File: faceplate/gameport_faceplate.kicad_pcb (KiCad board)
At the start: 2 copper layers, 25 x 200 mm, 5 parts

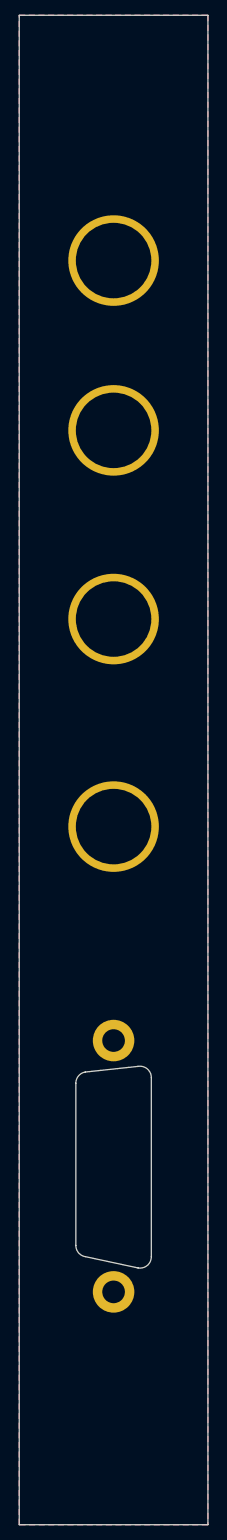
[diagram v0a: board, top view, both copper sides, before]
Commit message: Complete faceplate
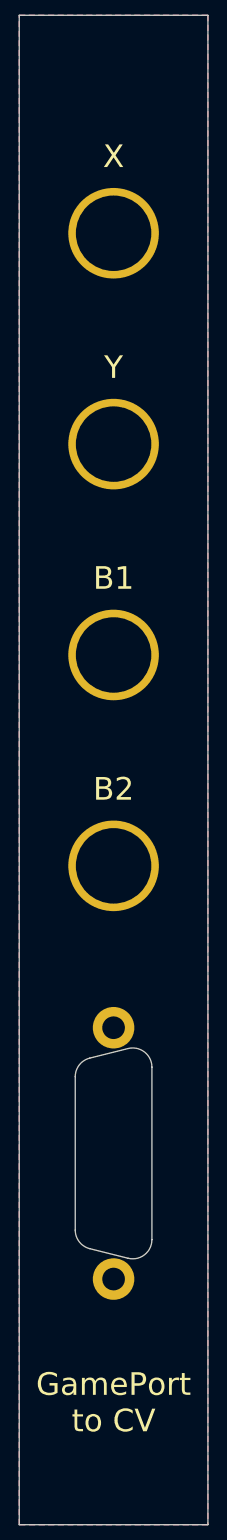
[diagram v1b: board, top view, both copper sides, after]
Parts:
- moved H4 5.20 mm to (112.5, 137.7)
- moved H3 4.76 mm to (112.5, 109.8)
- moved H1 3.62 mm to (112.5, 53.9)
- moved H2 1.82 mm to (112.5, 81.8)
- moved H5 1.70 mm to (112.5, 175.8)
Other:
- outline, holes or cut-outs redrawn
- board text added: "B1"
- board text added: "B2"
- board text added: "GamePort to CV"
- board text added: "JLCJLCJLCJLC"
- board text added: "X"
- board text added: "Y"
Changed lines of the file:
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@@
   (general
     (thickness 1.6)
-    (drawings 18)
+    (drawings 26)
     (tracks 0)
     (zones 0)
@@
   )
   (module modular:DSub_15_Cutout (layer F.Cu)
-    (at 112.5 177.5)
+    (at 112.5 175.8)
     (fp_text reference H5 (at 0 20) (layer F.SilkS) hide
       (effects (font (size 1 1) (thickness 0.15)))
@@
   )
   (module modular:Jack (layer F.Cu)
-    (at 112.5 132.5)
+    (at 112.5 137.7)
     (fp_text reference H4 (at 0 7.5) (layer F.SilkS) hide
       (effects (font (size 1 1) (thickness 0.15)))
@@
   )
   (module modular:Jack (layer F.Cu)
-    (at 112.5 105)
+    (at 112.5 109.76)
     (fp_text reference H3 (at 0 7.5) (layer F.SilkS) hide
       (effects (font (size 1 1) (thickness 0.15)))
@@
   )
   (module modular:Jack (layer F.Cu)
-    (at 112.5 80)
+    (at 112.5 81.82)
     (fp_text reference H2 (at 0 7.5) (layer F.SilkS) hide
       (effects (font (size 1 1) (thickness 0.15)))
@@
   )
   (module modular:Jack (layer F.Cu)
-    (at 112.5 57.5)
+    (at 112.5 53.88)
     (fp_text reference H1 (at 0 7.5) (layer F.SilkS) hide
       (effects (font (size 1 1) (thickness 0.15)))
@@
       (net 1 GND))
   )
-  (gr_line (start 100 177.5) (end 125 177.5) (layer Dwgs.User) (width 0.15))
-  (gr_arc (start 120.25 188.5) (end 122.25 188.5) (angle 100) (layer Dwgs.User) (width 0.05))
-  (gr_arc (start 116 165.75) (end 117.5 165.75) (angle -100) (layer Edge.Cuts) (width 0.05))
-  (gr_arc (start 109 166.5) (end 107.5 166.5) (angle 80) (layer Edge.Cuts) (width 0.05))
-  (gr_arc (start 109 188) (end 107.5 188) (angle -80) (layer Edge.Cuts) (width 0.05))
-  (gr_arc (start 116 189.5) (end 117.5 189.5) (angle 100) (layer Edge.Cuts) (width 0.05))
-  (gr_line (start 100 125) (end 125 125) (layer Dwgs.User) (width 0.15))
-  (gr_line (start 108.739528 165.022788) (end 115.739528 164.272788) (layer Edge.Cuts) (width 0.05))
-  (gr_line (start 107.5 188) (end 107.5 166.5) (layer Edge.Cuts) (width 0.05))
-  (gr_line (start 115.739528 190.977212) (end 108.739528 189.477212) (layer Edge.Cuts) (width 0.05))
-  (gr_line (start 117.5 165.75) (end 117.5 189.5) (layer Edge.Cuts) (width 0.05))
+  (gr_text JLCJLCJLCJLC (at 122.66 125 270) (layer B.SilkS)
+    (effects (font (size 1 1) (thickness 0.15)) (justify mirror))
+  )
+  (gr_text "GamePort\nto CV" (at 112.5 208.82) (layer F.SilkS)
+    (effects (font (size 3 3) (thickness 0.5)))
+  )
+  (gr_text B2 (at 112.5 127.54) (layer F.SilkS)
+    (effects (font (size 3 3) (thickness 0.45)))
+  )
+  (gr_text B1 (at 112.5 99.6) (layer F.SilkS)
+    (effects (font (size 3 3) (thickness 0.45)))
+  )
+  (gr_text Y (at 112.5 71.66) (layer F.SilkS)
+    (effects (font (size 3 3) (thickness 0.45)))
+  )
+  (gr_text X (at 112.5 43.72) (layer F.SilkS)
+    (effects (font (size 3 3) (thickness 0.45)))
+  )
+  (dimension 27.94 (width 0.15) (layer Dwgs.User)
+    (gr_text "1.1000 in" (at 121.42 175.8 90) (layer Dwgs.User)
+      (effects (font (size 1 1) (thickness 0.15)))
+    )
+    (feature1 (pts (xy 115.04 161.83) (xy 120.706421 161.83)))
+    (feature2 (pts (xy 115.04 189.77) (xy 120.706421 189.77)))
+    (crossbar (pts (xy 120.12 189.77) (xy 120.12 161.83)))
+    (arrow1a (pts (xy 120.12 161.83) (xy 120.706421 162.956504)))
+    (arrow1b (pts (xy 120.12 161.83) (xy 119.533579 162.956504)))
+    (arrow2a (pts (xy 120.12 189.77) (xy 120.706421 188.643496)))
+    (arrow2b (pts (xy 120.12 189.77) (xy 119.533579 188.643496)))
+  )
+  (dimension 33.02 (width 0.15) (layer Dwgs.User)
+    (gr_text "1.3000 in" (at 103.58 175.8 90) (layer Dwgs.User)
+      (effects (font (size 1 1) (thickness 0.15)))
+    )
+    (feature1 (pts (xy 112.5 159.29) (xy 104.293579 159.29)))
+    (feature2 (pts (xy 112.5 192.31) (xy 104.293579 192.31)))
+    (crossbar (pts (xy 104.88 192.31) (xy 104.88 159.29)))
+    (arrow1a (pts (xy 104.88 159.29) (xy 105.466421 160.416504)))
+    (arrow1b (pts (xy 104.88 159.29) (xy 104.293579 160.416504)))
+    (arrow2a (pts (xy 104.88 192.31) (xy 105.466421 191.183496)))
+    (arrow2b (pts (xy 104.88 192.31) (xy 104.293579 191.183496)))
+  )
+  (gr_line (start 109.343961 163.175839) (end 114.42396 161.905838) (layer Edge.Cuts) (width 0.05))
+  (gr_arc (start 109.96 165.64) (end 109.343961 163.175839) (angle -75.96376747) (layer Edge.Cuts) (width 0.05))
+  (gr_arc (start 115.04 164.37) (end 117.58 164.37) (angle -104.0362435) (layer Edge.Cuts) (width 0.05))
+  (gr_line (start 109.345518 188.424551) (end 114.423961 189.694161) (layer Edge.Cuts) (width 0.05))
+  (gr_arc (start 115.04 187.23) (end 114.423961 189.694161) (angle -104.0362325) (layer Edge.Cuts) (width 0.05))
+  (gr_arc (start 109.96 185.96) (end 107.42 185.96) (angle -75.99999078) (layer Edge.Cuts) (width 0.05))
+  (dimension 10.16 (width 0.15) (layer Dwgs.User)
+    (gr_text "0.4000 in" (at 112.5 208.85) (layer Dwgs.User)
+      (effects (font (size 1 1) (thickness 0.15)))
+    )
+    (feature1 (pts (xy 117.58 191.04) (xy 117.58 208.136421)))
+    (feature2 (pts (xy 107.42 191.04) (xy 107.42 208.136421)))
+    (crossbar (pts (xy 107.42 207.55) (xy 117.58 207.55)))
+    (arrow1a (pts (xy 117.58 207.55) (xy 116.453496 208.136421)))
+    (arrow1b (pts (xy 117.58 207.55) (xy 116.453496 206.963579)))
+    (arrow2a (pts (xy 107.42 207.55) (xy 108.546504 208.136421)))
+    (arrow2b (pts (xy 107.42 207.55) (xy 108.546504 206.963579)))
+  )
+  (gr_line (start 100 175.8) (end 125 175.8) (layer Dwgs.User) (width 0.15))
+  (gr_line (start 100.2 125) (end 125.2 125) (layer Dwgs.User) (width 0.15))
+  (gr_line (start 107.42 185.96) (end 107.42 165.64) (layer Edge.Cuts) (width 0.05))
+  (gr_line (start 117.58 164.37) (end 117.579999 187.229999) (layer Edge.Cuts) (width 0.05))
   (gr_line (start 100 35) (end 125 35) (layer Dwgs.User) (width 0.15))
   (gr_line (start 100 215) (end 125 215) (layer Dwgs.User) (width 0.15))
